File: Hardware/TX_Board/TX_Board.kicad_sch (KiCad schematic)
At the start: 48 parts, among them IC1 GP2Y1+, IC2 GP2Y1+, IC3 GP2Y1+, IC4 LT3041ADE#PBF, IC5 LT3099ADE#PBF, IC6 ADPL40502AUJZ-1.5-R7, J1 Conn_Coaxial, J10 MM8030-2610RJ3, J11 MM8030-2610RJ3, J12 MM8030-2610RJ3, J2 Conn_01x01_Pin, J3 Conn_01x01_Pin, J4 Conn_01x01_Pin, J5 Conn_01x01_Pin, J6 Conn_02x12_Odd_Even, J7 Conn_01x03_Socket, J8 Conn_02x08_Odd_Even, J9 MM8030-2610RJ3, U1 SN74HCT138NSR

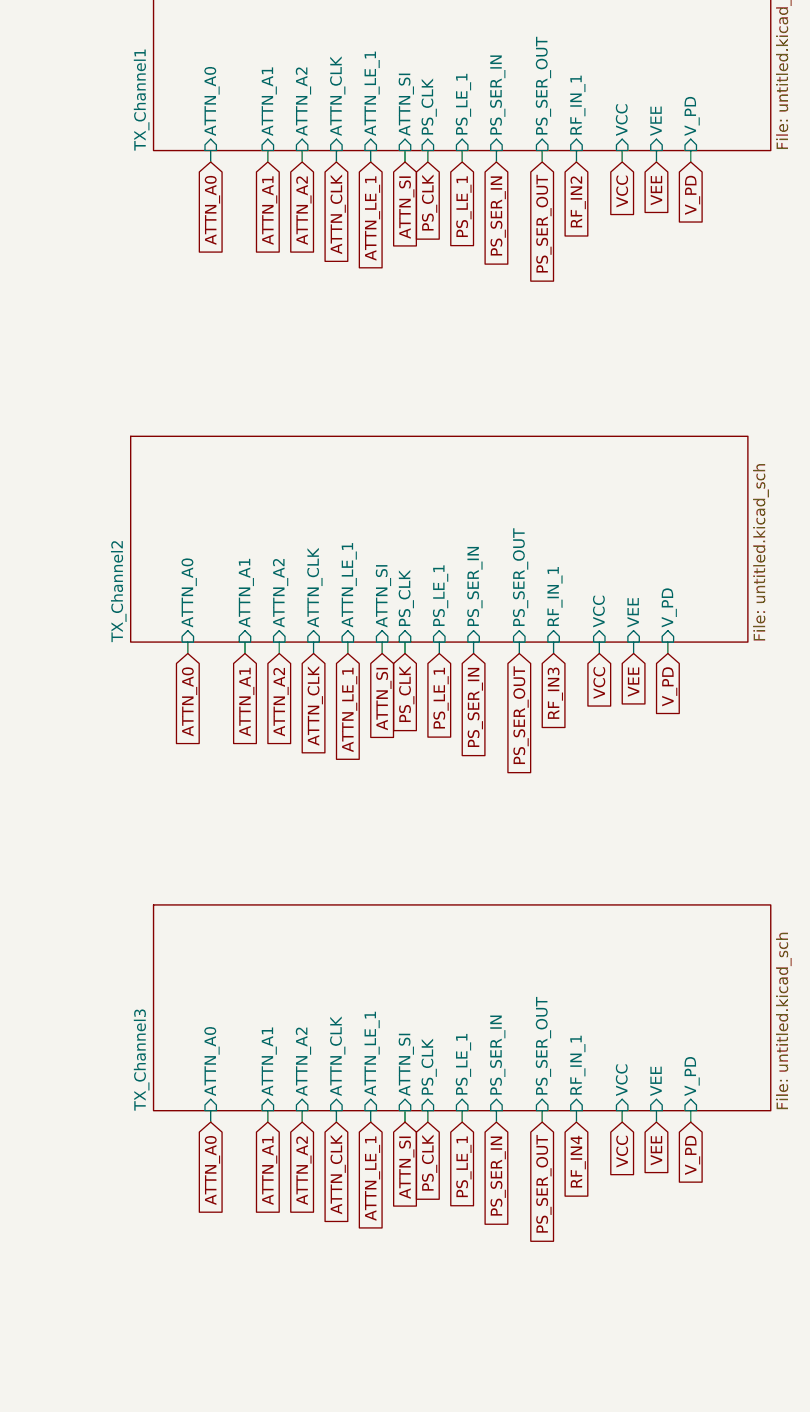
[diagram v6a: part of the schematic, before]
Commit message: rough layout using replicate plugin
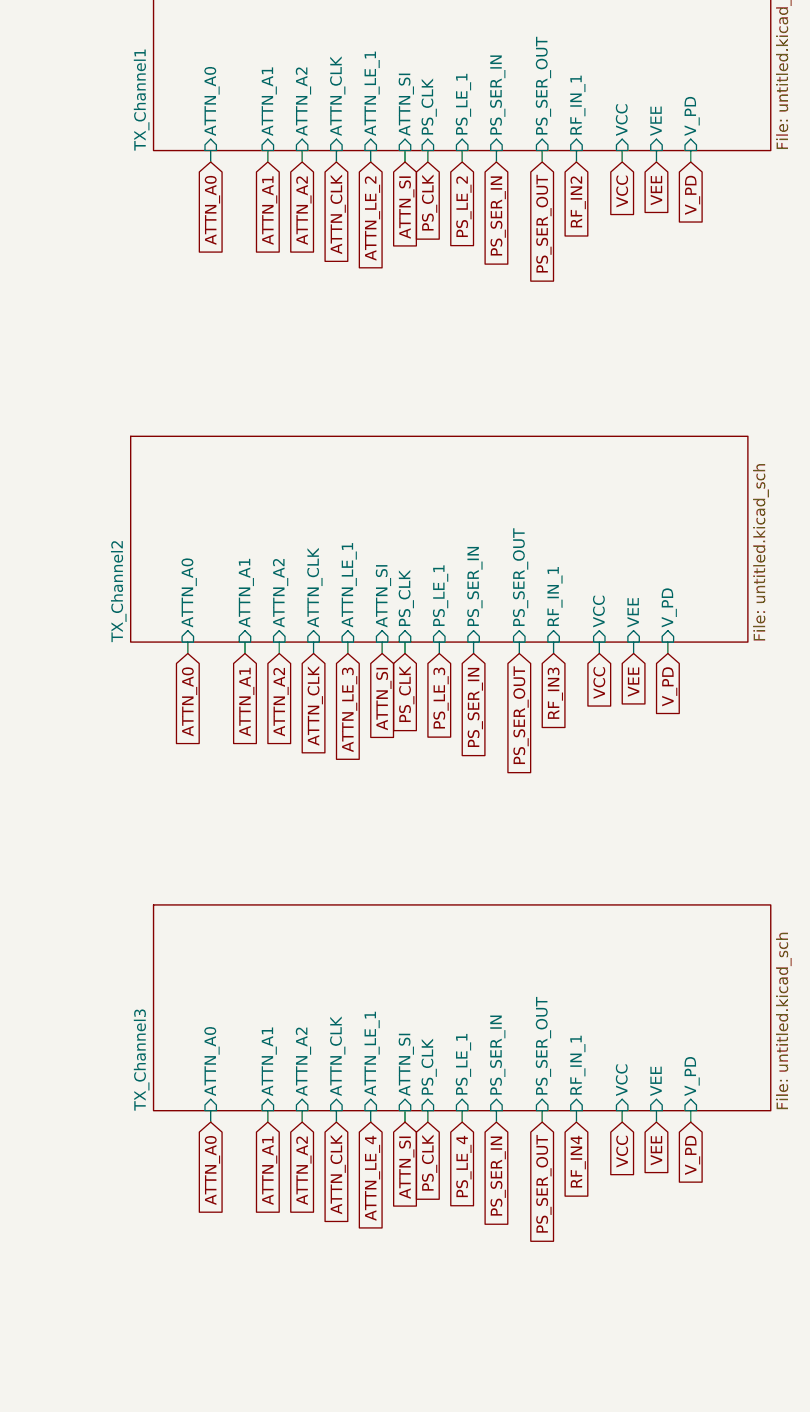
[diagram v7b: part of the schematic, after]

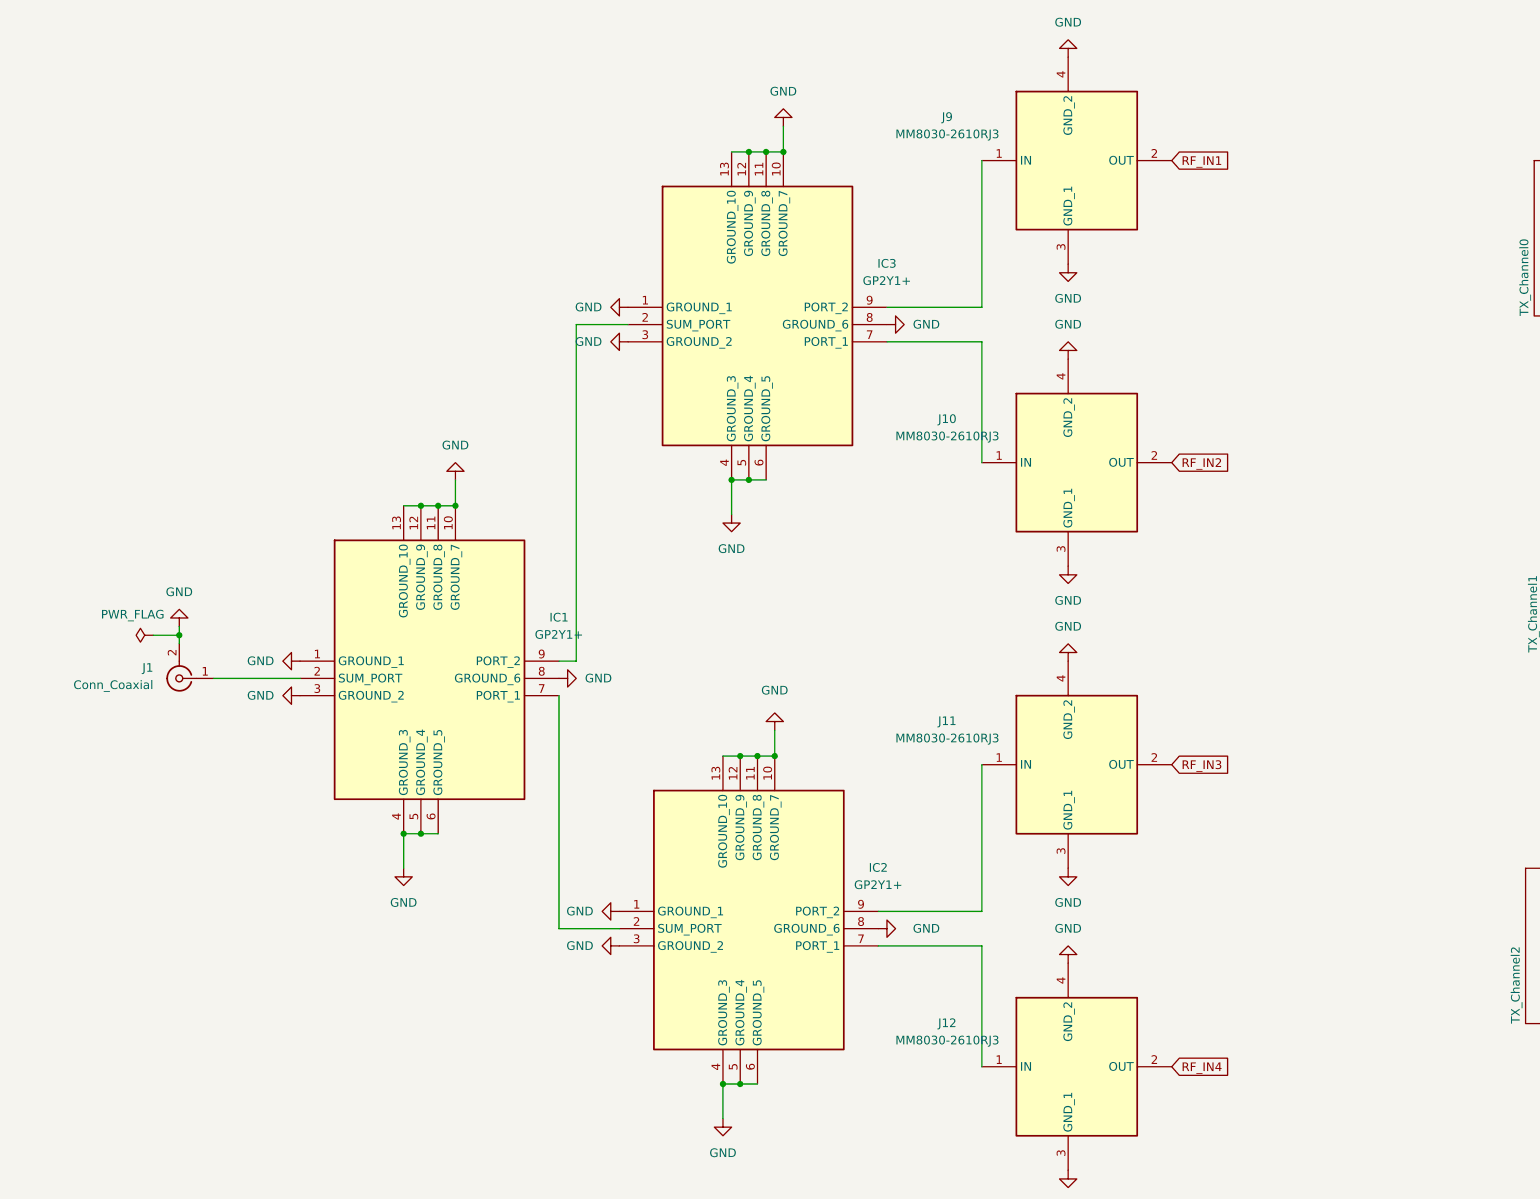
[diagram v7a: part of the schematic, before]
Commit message: Waveguide + ground planes and P.S. daughter board modification
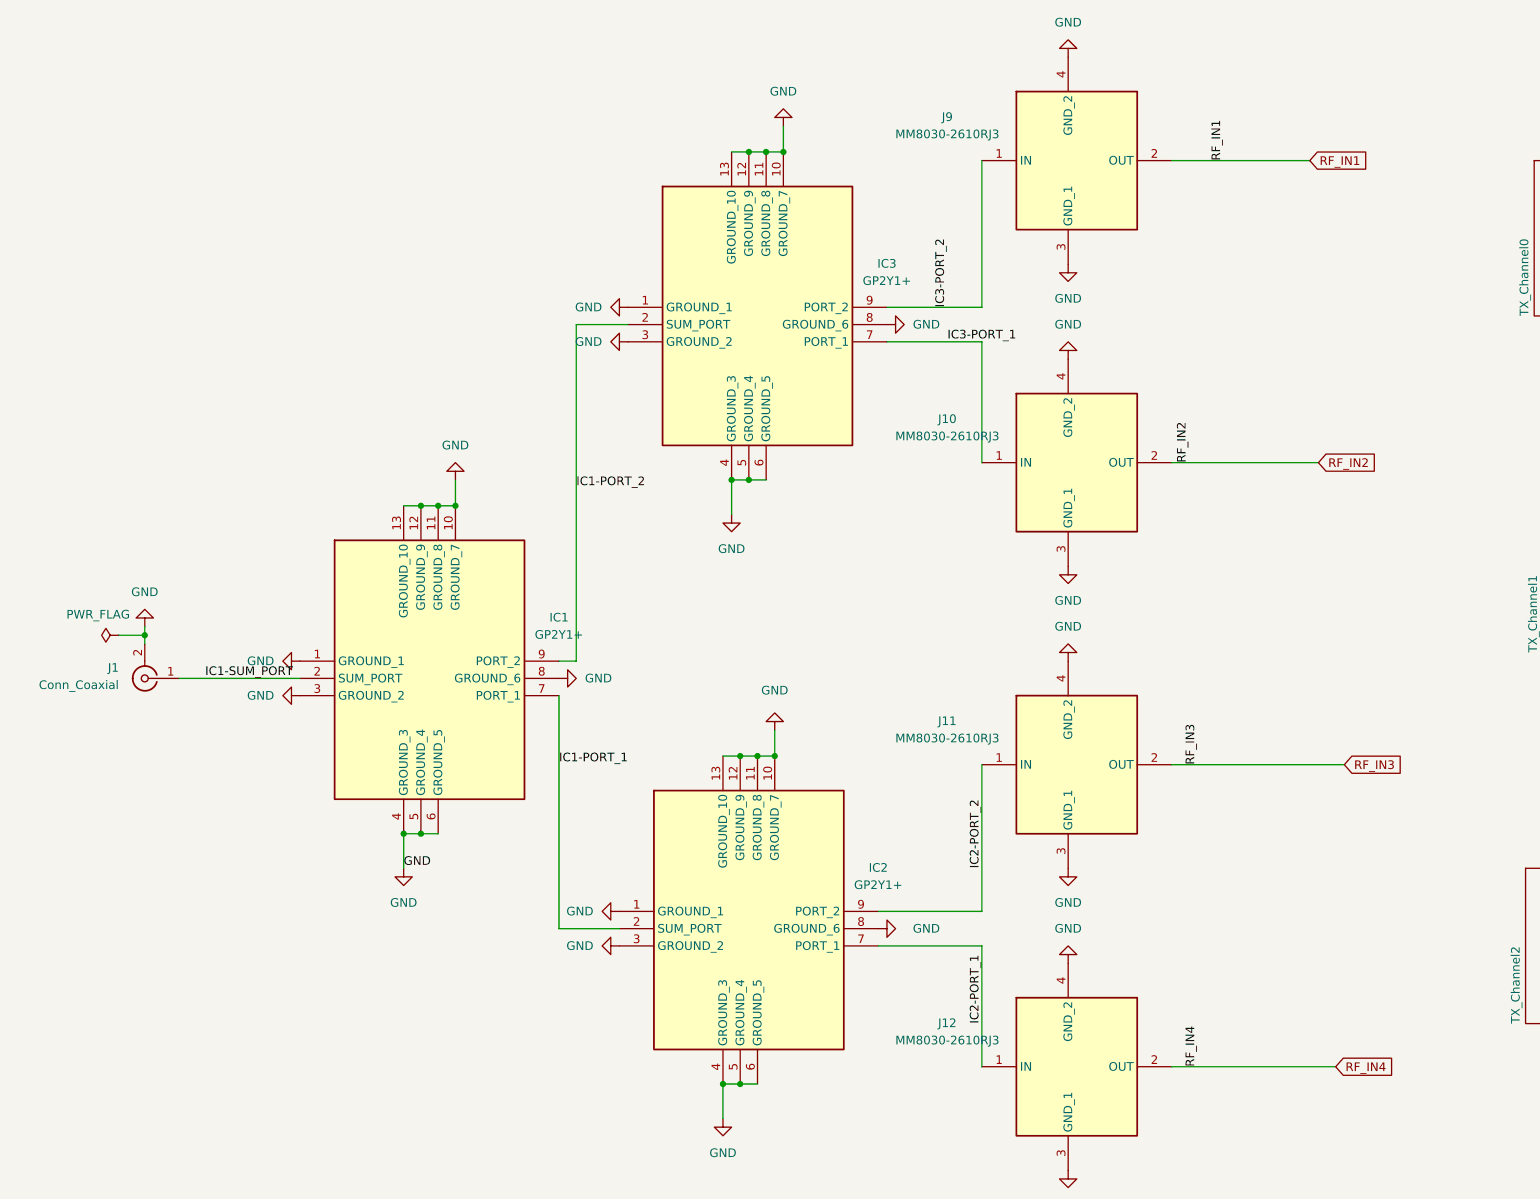
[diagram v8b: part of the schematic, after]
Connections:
- net IC1-SUM_PORT: now reaches IC1.2 (SUM_PORT), J1.1 (In)
- net IC1-PORT_1: now reaches IC1.7 (PORT_1), IC2.2 (SUM_PORT)
- net IC1-PORT_2: now reaches IC1.9 (PORT_2), IC3.2 (SUM_PORT)
- net IC3-PORT_1: now reaches IC3.7 (PORT_1), J10.1 (IN)
- net IC3-PORT_2: now reaches IC3.9 (PORT_2), J9.1 (IN)
- net IC2-PORT_1: now reaches IC2.7 (PORT_1), J12.1 (IN)
- net IC2-PORT_2: now reaches IC2.9 (PORT_2), J11.1 (IN)
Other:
- moved on the sheet: J1
